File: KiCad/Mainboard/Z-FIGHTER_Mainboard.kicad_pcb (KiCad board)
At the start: 2 copper layers, 100 x 150 mm, 55 parts, among them IC1 Z80SIO, J1 DB9_Male_MountingHoles, J2 DB9_Male_MountingHoles, J3 USB_B, J4 Conn_02x13_Odd_Even, J5 Conn_Parallel_User, J6 Conn_PATA, J7 Conn_02x03_Odd_Even, SW1 SW_Push, SW2 SW_DIP_x03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

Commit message: Changed accessory parallel header footprint and silkscreen
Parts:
- J4: footprint Connector_IDC:IDC-Header_2x13_P2.54mm_Vertical -> Connector_PinHeader_2.54mm:PinHeader_2x13_P2.54mm_Vertical

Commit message: Routing
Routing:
- net VCC: track 161.4 -> 173.4 mm

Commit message: A13
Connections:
- U7 pad 3: GND -> A13
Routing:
- net A13: track 70.2 -> 74.0 mm
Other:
- board text added: "Mainboard Rev. 2d"
- board text removed: "Mainboard Rev. 2c"
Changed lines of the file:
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@@
     (thickness 1.6)
     (drawings 34)
-    (tracks 1729)
+    (tracks 1738)
     (zones 0)
     (modules 55)
@@
       (net 112 "#ROMD_OUT"))
     (pad 3 thru_hole oval (at 0 5.08 90) (size 1.6 1.6) (drill 0.8) (layers *.Cu *.Mask)
-      (net 135 GND))
+      (net 103 A13))
     (pad 15 thru_hole oval (at 7.62 22.86 90) (size 1.6 1.6) (drill 0.8) (layers *.Cu *.Mask)
       (net 110 "#ROMCS"))
@@
     (effects (font (size 1 1) (thickness 0.15)))
   )
-  (gr_text "Mainboard Rev. 2c" (at 124.944514 51.6114) (layer B.SilkS)
+  (gr_text "Mainboard Rev. 2d" (at 124.9088 51.6114) (layer B.SilkS)
     (effects (font (size 1.5 1.5) (thickness 0.2)) (justify mirror))
   )
@@
   (segment (start 101.7536 77.867798) (end 99.24059 77.867798) (width 0.2032) (layer B.Cu) (net 103))
   (segment (start 101.8536 77.767798) (end 101.7536 77.867798) (width 0.2032) (layer B.Cu) (net 103))
-  (segment (start 99.1436 106.1958) (end 99.1436 77.770808) (width 0.2032) (layer F.Cu) (net 103))
   (segment (start 97.9836 107.3558) (end 99.1436 106.1958) (width 0.2032) (layer F.Cu) (net 103) (status 10))
+  (segment (start 97.97 88.0739) (end 97.9836 88.0875) (width 0.762) (layer F.Cu) (net 103) (status 30))
+  (segment (start 99.1269 88.0875) (end 99.1436 88.0708) (width 0.2032) (layer F.Cu) (net 103))
+  (segment (start 97.9836 88.0875) (end 99.1269 88.0875) (width 0.2032) (layer F.Cu) (net 103))
+  (segment (start 98.8069 88.0875) (end 99.1436 87.7508) (width 0.2032) (layer F.Cu) (net 103))
+  (segment (start 97.9836 88.0875) (end 98.8069 88.0875) (width 0.2032) (layer F.Cu) (net 103))
+  (segment (start 99.1436 87.7508) (end 99.1436 77.770808) (width 0.2032) (layer F.Cu) (net 103))
+  (segment (start 99.1436 88.0708) (end 99.1436 87.7508) (width 0.2032) (layer F.Cu) (net 103))
+  (segment (start 98.8303 88.0875) (end 99.1436 88.4008) (width 0.2032) (layer F.Cu) (net 103))
+  (segment (start 97.9836 88.0875) (end 98.8303 88.0875) (width 0.2032) (layer F.Cu) (net 103))
+  (segment (start 99.1436 88.4008) (end 99.1436 88.0708) (width 0.2032) (layer F.Cu) (net 103))
+  (segment (start 99.1436 106.1958) (end 99.1436 88.4008) (width 0.2032) (layer F.Cu) (net 103))
   (via (at 94.1336 100.865) (size 0.508) (drill 0.3302) (layers F.Cu B.Cu) (net 104))
   (via (at 103.0636 100.865) (size 0.508) (drill 0.3302) (layers F.Cu B.Cu) (net 104))
@@
   (segment (start 87.9036 116.0508) (end 88.133399 115.821001) (width 0.762) (layer B.Cu) (net 135) (status 30))
   (segment (start 87.9036 52.1258) (end 87.9036 52.2508) (width 0.762) (layer F.Cu) (net 135) (status 30))
-  (segment (start 97.97 88.0739) (end 97.9836 88.0875) (width 0.762) (layer F.Cu) (net 135) (status 30))
   (via (at 108.15 140.38) (size 0.9398) (drill 0.5334) (layers F.Cu B.Cu) (net 135))
   (segment (start 108.1436 140.3864) (end 108.15 140.38) (width 0.762) (layer F.Cu) (net 135))

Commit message: Initial commit
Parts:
- J7: value Conn_02x03_Odd_Even -> Conn_02x04_Odd_Even; footprint Connector_IDC:IDC-Header_2x03_P2.54mm_Horizontal -> Connector_IDC:IDC-Header_2x04_P2.54mm_Horizontal
- moved REF** 2.07 mm to (71.7, 94.0)
- moved X1 2.07 mm to (71.7, 86.4)
- moved REF** 1.25 mm to (71.7, 72.4)
- moved X2 1.25 mm to (71.7, 64.8)
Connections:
- U2 pad 18: Net-(U2-Pad18) -> HALT
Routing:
- net #RESET: track 141.0 -> 207.5 mm, vias 5 -> 7
- net CLOCK2: track 28.3 -> 0.18 mm
- net CLOCK: track 123.7 -> 120.7 mm, vias 1 -> 2
- net #WAIT: track 80.8 -> 79.8 mm
- net #NMI: track 62.8 -> 62.1 mm
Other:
- board text added: "Mainboard Rev. 2e"
- board text removed: "Mainboard Rev. 2d"

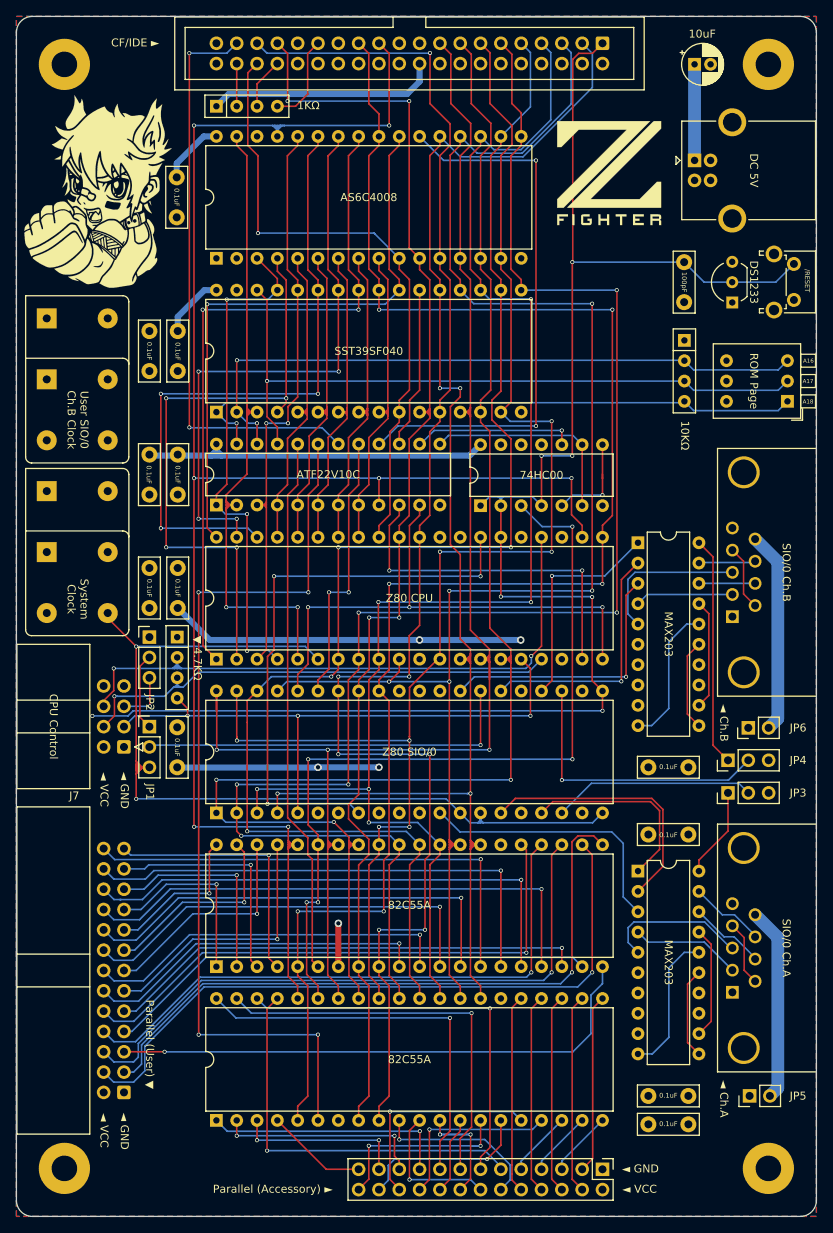
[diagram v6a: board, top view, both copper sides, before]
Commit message: Case adjustment, schema update, layout image update, readme
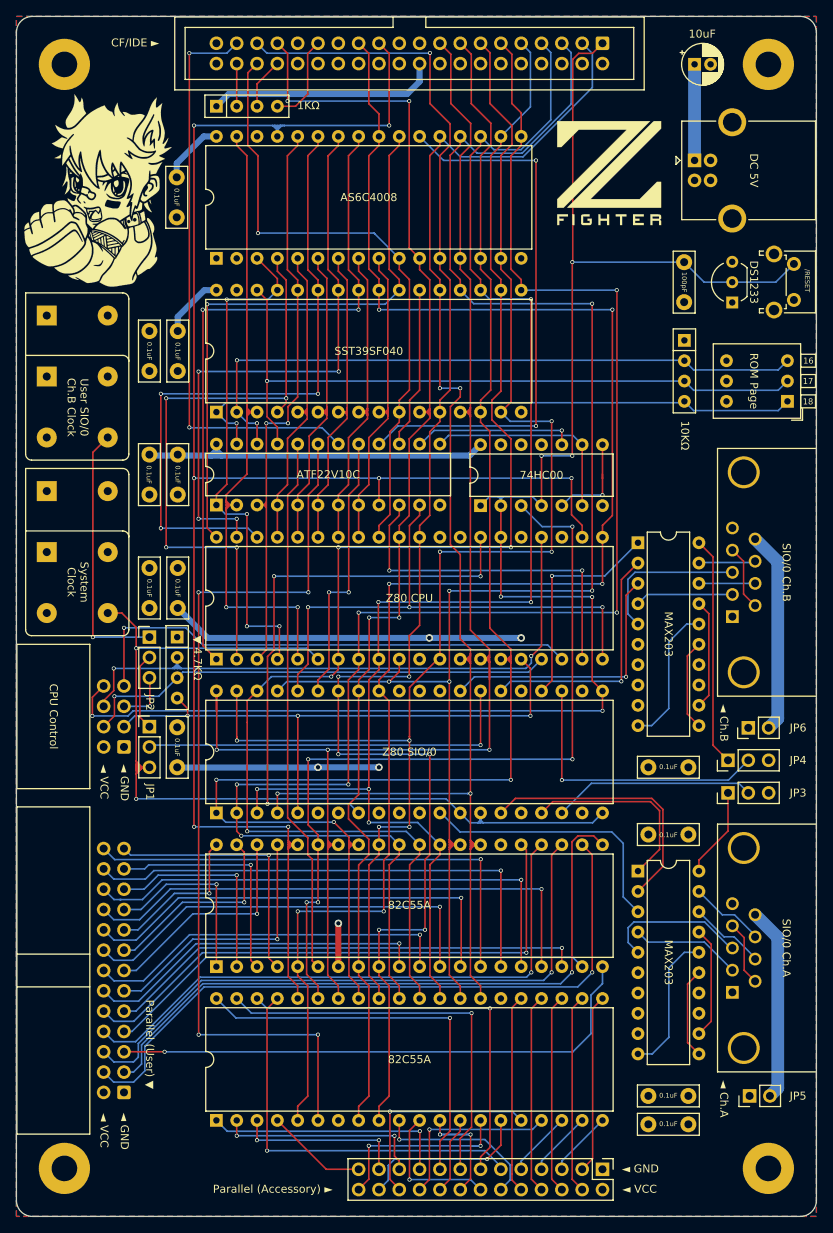
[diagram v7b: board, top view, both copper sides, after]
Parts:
- moved X2 0.36 mm to (71.7, 64.4)
- moved REF** 0.36 mm to (71.7, 72.0)
- moved G*** 0.14 mm to (78.3, 48.6)
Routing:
- net HALT: track 0.00 -> 63.6 mm, vias 0 -> 1
- net CLOCK2: track 0.18 -> 32.3 mm, vias 0 -> 1
- net #RESET: track 207.5 -> 211.8 mm
- net #NMI: track 62.1 -> 59.7 mm
- net CLOCK: track 120.7 -> 122.2 mm
- net A14: track 63.7 -> 65.0 mm, vias 3 -> 4
- net #WAIT: track 79.8 -> 79.1 mm
- net #INT: track 74.5 -> 73.9 mm
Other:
- board text added: "16"
- board text added: "17"
- board text added: "18"
- board text removed: "A16"
- board text removed: "A17"
- board text removed: "A18"
